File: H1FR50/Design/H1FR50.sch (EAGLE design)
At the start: 49 parts, among them P1 HEXABIT_17.32_NO_P6, U1 STM32F091CBU6, U2 TPS22943DCKR, U3 BGA824N6, U4 TESEO-LIV3F, U5 B39162B4327P810, X1 XTALL_CSTCE8M00G52

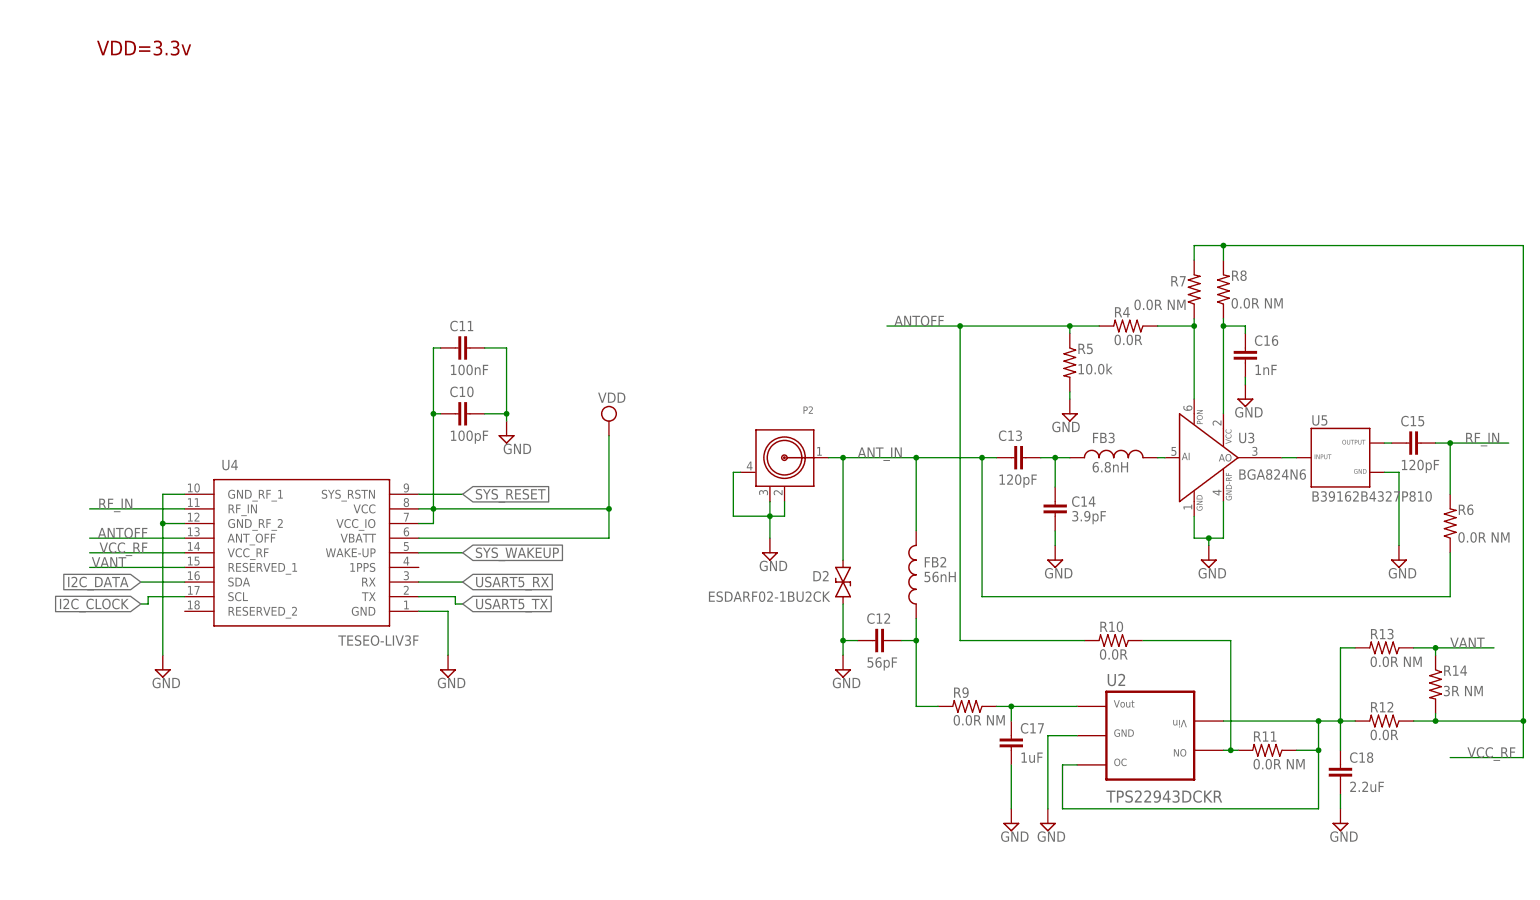
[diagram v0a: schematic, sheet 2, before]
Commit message: - Rearanged all P#.. - Removed Keepout areas.. - Renamed all NM to DNP.. - Moved D1 from layer 16 to layer 1.. - Changed R8 from 0R NM to 0R.. - Placed more Grounding vias around RF connector in brd.. - Added two pullups res on I2C lines.. - Added the recomended filters on Tevo's power pins.. - Updated Document.. - Updated BOM..
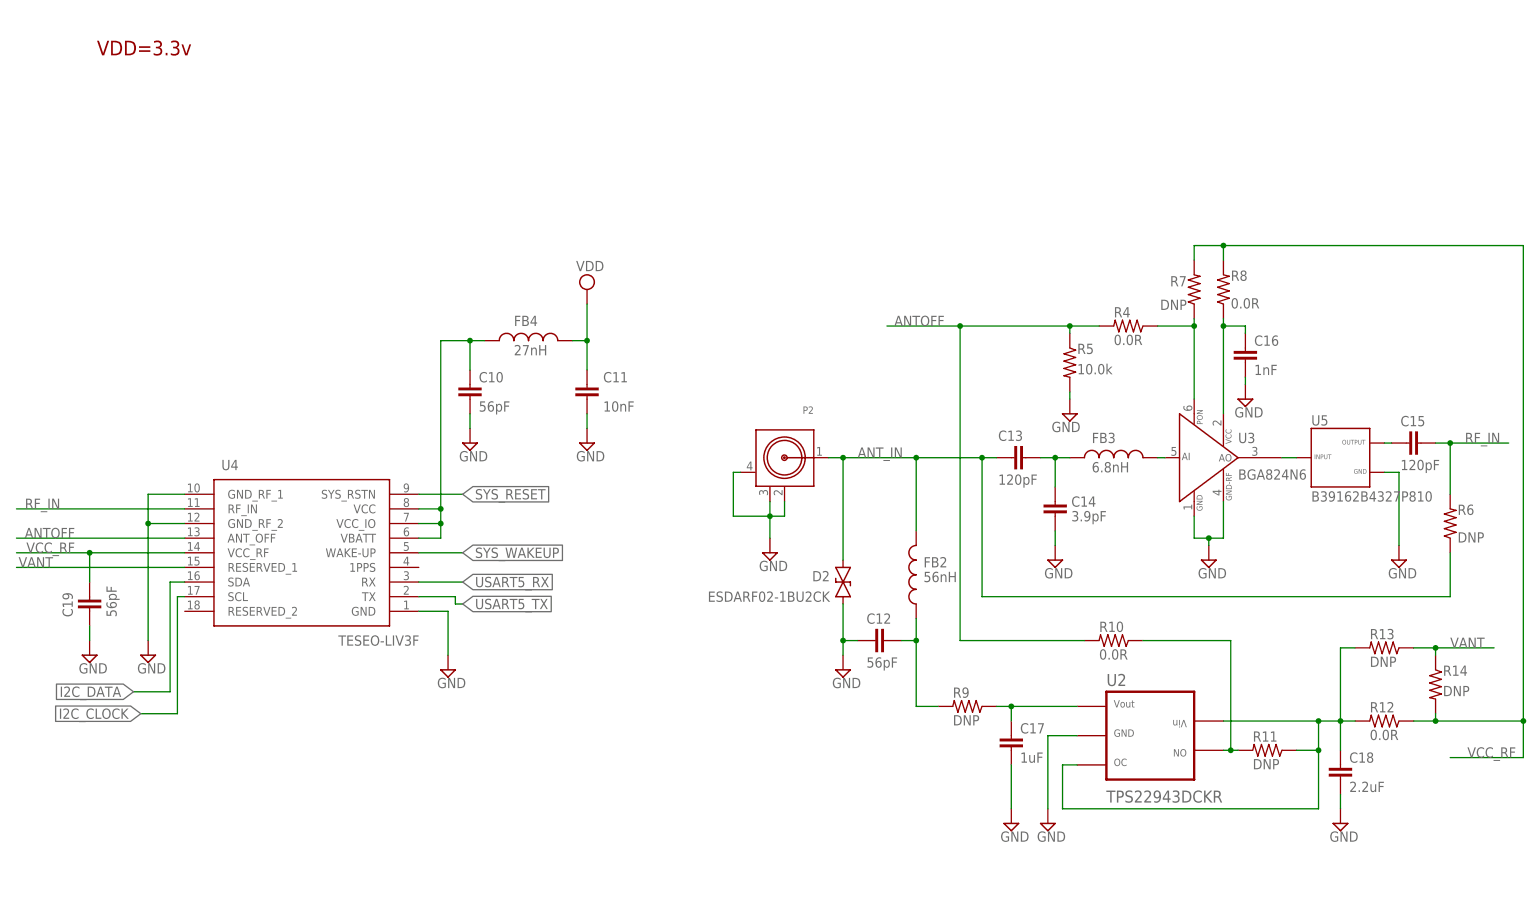
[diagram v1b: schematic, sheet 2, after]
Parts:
- added C19: 56pF, HEXABITZ_RCLS:C-0402
- added FB4: 27nH, HEXABITZ_RCLS:FB-0402
- added R15, R16: 2.2k, HEXABITZ_RCLS:R-0402
- C10: value 100pF -> 56pF
- C11: value 100nF -> 10nF
- R11, R13, R6, R7, R9: value 0.0R NM -> DNP
- R14: value 3R NM -> DNP
- R8: value 0.0R NM -> 0.0R
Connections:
- new net VCC_RF1: C10.2, FB4.1, U4.VBATT, U4.VCC, U4.VCC_IO
- net GND: now also C10.1, C11.1, C19.1; no longer C10.2, C11.2
- net I2C_CLOCK: now also R15.2
- net I2C_DATA: now also R16.2
- net VCC_RF: now also C19.2
- net VDD: now also C11.2, FB4.2, R15.1, R16.1; no longer C10.1, C11.1, U4.VBATT, U4.VCC, U4.VCC_IO
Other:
- moved on the sheet: C10, C11

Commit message: - Redesigned both Schematic and PCB.. - Updated BOM and Documentation..
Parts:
- removed FB1: FB-TDK_MMZ1608Y300B, Hexabitz:FB-TDK_MMZ1608Y300B
- removed R15, R16: 2.2k, HEXABITZ_RCLS:R-0402
- removed R3: 0.0R, Hexabitz:R-0603
- C1: value 100nF -> 10nF; CAPACITANCE 100nF -> 10nF; MFN AVX -> KEMET; MPN 0603YC104K4T2A -> C0603C103K5RACTU; OCTOPART_URL https://octopart.com/c0603c104k8ractu-kemet-145075?r=sp&s=9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 -> https://octopart.com/c0603c103k5ractu-kemet-133094?r=sp&s=R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; VOLTAGE_RATING 16V -> 50V
- C10, C19: device HEXABITZ_RCLS:C-0402 -> HEXABITZ_RCLS:C-0201C0201; MFN (none) -> Murata; MPN (none) -> GRM0335C1E560GA01D; OCTOPART_URL (none) -> https://octopart.com/grm0335c1e560ga01d-murata-24611383?r=sp
- C11: CAPACITANCE (none) -> 10nF; MFN (none) -> TDK; MPN (none) -> CGA2B3X7R1H103K050BE; OCTOPART_URL (none) -> https://octopart.com/cga2b3x7r1h103k050be-tdk-68305469?r=sp
- C12: CAPACITANCE (none) -> 56pF; MFN (none) -> Murata; MPN (none) -> GRM1555C1H560JA01D; OCTOPART_URL (none) -> https://octopart.com/grm1555c1h560ja01d-murata-15197568?r=sp
- C13, C15: CAPACITANCE (none) -> 120pF; MFN (none) -> Murata; MPN (none) -> GRM1555C1H121JA01D; OCTOPART_URL (none) -> https://octopart.com/grm1555c1h121ja01d-murata-196010?r=sp
- C14: CAPACITANCE (none) -> 3.9pF; MFN (none) -> Murata; MPN (none) -> GRM1555C1H3R9WA01D; OCTOPART_URL (none) -> https://octopart.com/grm1555c1h3r9wa01d-murata-20477997?r=sp
- C16: CAPACITANCE (none) -> 1nF; MFN (none) -> Murata; MPN (none) -> GRM155R71H102KA01D; OCTOPART_URL (none) -> https://octopart.com/grm155r71h102ka01d-murata-196021?r=sp
- C17: value 1uF -> 1.00uF; CAPACITANCE (none) -> 1.00uF; MFN (none) -> KEMET; MPN (none) -> C0402C105K8PAC7411; OCTOPART_URL (none) -> https://octopart.com/c0402c105k8pac7411-kemet-75146233?r=sp
- C18: CAPACITANCE (none) -> 2.2uF; MFN (none) -> https://octopart.com/c0402c225k7pactu-kemet-89187402?r=sp; MPN (none) -> C0402C225K7PACTU; OCTOPART_URL (none) -> https://octopart.com/c0402c225k7pactu-kemet-89187402?r=sp
- C2: MFN AVX -> Yageo; MPN TAJR105M016RNJ -> CC0805KKX7R7BB105; OCTOPART_URL https://octopart.com/tajr105m016rnj-avx-1188552 -> https://octopart.com/cc0805kkx7r7bb105-yageo-8376555?r=sp&s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; TOLERANCE 20% -> 10%
- C3: value 4.7uF -> 100nF; device Hexabitz:C-0805-POL -> Hexabitz:C-0603; CAPACITANCE 4.7uF -> 100nF; MFN Panasonic -> KEMET; MPN 10TPU4R7MSI -> C0603C104K8RACTU; OCTOPART_URL https://octopart.com/10tpu4r7msi-panasonic-29487748 -> https://octopart.com/c0603c104k8ractu-kemet-145075?r=sp&s=9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; TOLERANCE 20% -> 10%
- C4: MFN Panasonic -> Murata; MPN 10TPU4R7MSI -> GRM21BC81E475KA12L; OCTOPART_URL https://octopart.com/10tpu4r7msi-panasonic-29487748 -> https://octopart.com/grm21bc81e475ka12l-murata-10331911?r=s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; TOLERANCE 20% -> 10%; VOLTAGE_RATING 10V -> 25V
- C5: value 10nF -> 100nF; CAPACITANCE 10nF -> 100nF; MFN AVX -> KEMET; MPN 0603YC103KAT4A -> C0603C104K8RACTU; OCTOPART_URL https://octopart.com/0603yc103kat4a-avx-2550362 -> https://octopart.com/c0603c104k8ractu-kemet-145075?r=sp&s=9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; VOLTAGE_RATING 16V -> 10
- C6, C8: MFN AVX -> KEMET; MPN 0603YC104K4T2A -> C0603C104K8RACTU; OCTOPART_URL https://octopart.com/0603yc104k4t2a-avx-8120651# -> https://octopart.com/c0603c104k8ractu-kemet-145075?r=sp&s=9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; VOLTAGE_RATING 16V -> 10V
- C7: value 100nF -> 4.7uF; device Hexabitz:C-0603 -> Hexabitz:C-0805-POL; CAPACITANCE 100nF -> 4.7uF; MFN AVX -> Murata; MPN 0603YC104K4T2A -> GRM21BC81E475KA12L; OCTOPART_URL https://octopart.com/0603yc104k4t2a-avx-8120651# -> https://octopart.com/grm21bc81e475ka12l-murata-10331911?r=s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; VOLTAGE_RATING 16V -> 25V
- C9: MFN AVX -> KEMET; MPN 0603YC104K4T2A -> C0603C104K8RACTU; OCTOPART_URL https://octopart.com/0603yc104k4t2a-avx-8120651# -> https://octopart.com/c0603c104k8ractu-kemet-145075?r=sp&s=9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; TOLERANCE 10% -> 10V; VOLTAGE_RATING 16V -> 10%
- FB2: MFN (none) -> Murata; MPN (none) -> LQW15AN6N8G00D; OCTOPART_URL (none) -> https://octopart.com/lqw15an6n8g00d-murata-7896134?r=sp
- FB3: MFN (none) -> Würth Elektronik; MPN (none) -> 744784156A; OCTOPART_URL (none) -> https://octopart.com/744784156a-w%C3%BCrth+elektronik-46756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
- FB4: MFN (none) -> Murata; MPN (none) -> LQG15HS27NJ02D; OCTOPART_URL (none) -> https://octopart.com/lqg15hs27nj02d-murata-387555?r=sp
- P1: value HEXABIT_17.32_NO_P6 -> HEXABIT_17.32_X2_NO_P5; device hexabitz_connectors:HEXABIT_17.32_NO_P6 -> hexabitz_connectors:HEXABIT_17.32_X2_NO_P5
- R14: value DNP -> 100k; device HEXABITZ_RCLS:R-0402 -> HEXABITZ_RCLS:R-0603; MFN (none) -> Yageo; MPN (none) -> AC0603FR-07100KL; OCTOPART_URL (none) -> https://octopart.com/ac0603fr-07100kl-yageo-21711090?r=sp; RESISTANCE (none) -> 100k; TOLERANCE (none) -> ±1%
- R2: MFN Vishay -> Yageo; MPN CRCW060310K0JNEB -> RC0603JR-0710KL; OCTOPART_URL https://octopart.com/crcw060310k0jneb-vishay-46603269 -> https://octopart.com/search?q=RC0603JR-0710KL&start=0
- R5: MFN (none) -> TE Connectivity; MPN (none) -> CRGCQ0402F10K; OCTOPART_URL (none) -> https://octopart.com/crgcq0402f10k-te+connectivity-91017932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; RESISTANCE (none) -> 10.0K; TOLERANCE (none) -> ±1%
- U1: value STM32F091CBU6 -> STM32F091RBT6STMICROELECTRONICS_STM32F091RBT6_0_1; device Hexabitz:STM32F091CBU6 -> Hexabitz:STM32F091RBT6STMICROELECTRONICS_STM32F091RBT6_0_1; MFN (none) -> STMicroelectronics; OCTOPART_URL (none) -> https://octopart.com/stm32f091rbt6-stmicroelectronics-51988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
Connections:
- removed net USART1_RX: P1.SD5, U1.PA10
- removed net USART1_TX: P1.SU5, U1.PA9
- removed net USART2_RX: P1.SD2, U1.PA3
- removed net USART2_TX: P1.SU2, U1.PA2
- removed net USART3_RX: P1.SD4, U1.PB11
- removed net USART3_TX: P1.SU4, U1.PB10
- removed net USART4_RX: P1.SD1, U1.PA1
- removed net USART4_TX: P1.SU1, U1.PA0
- removed net USART5_RX: U1.PB4, U4.RX
- removed net USART5_TX: U1.PB3, U4.TX
- removed net USART6_RX: P1.SD3, U1.PA5
- removed net USART6_TX: P1.SU3, U1.PA4
- removed net VANT: R13.1, R14.1, U4.RESERVED_1
- removed net VDDA: C2.+, C5.1, FB1.1, U1.VDDA
- removed net VSSA: C2.-, C5.2, R3.2, U1.VSS_A
- new net N$2: R14.2, U2.OC
- new net N$3: C13.1, D2.2, FB2.2, P2.1, R13.2
- new net UART1_RX*: P1.SD7, U1.PA10
- new net UART1_TX*: P1.SU7, U1.PA9
- new net UART2_RX*: P1.SD3, U1.PA3
- new net UART2_TX*: P1.SU3, U1.PA2
- new net UART3_RX: U1.PB11, U4.RX
- new net UART3_TX: U1.PB10, U4.TX
- new net UART4_RX: P1.SD2, U1.PA1
- new net UART4_TX: P1.SU2, U1.PA0
- new net UART5_RX: P1.SD8, U1.PB4
- new net UART5_TX: P1.SU8, U1.PB3
- new net UART6_RX: P1.SD10, U1.PA5
- new net UART6_TX: P1.SU10, U1.PA4
- new net UART7_RX: P1.SD9, U1.PC1
- new net UART7_TX: P1.SU9, U1.PC0
- new net UART8_RX: P1.SD1, U1.PC3
- new net UART8_TX: P1.SU1, U1.PC2
- net ANT_IN: now also R13.1; no longer C13.1, D2.2, FB2.2, P2.1
- net B1: now also U1.PF11-BOOT0; no longer U1.PF11-OSC_BOOT0
- net GND: now also C2.-, C3.2, C5.2, C7.-, P1.GND10, P1.GND7, P1.GND9, U1.1_VSS, U1.2_VSS, U1.3_VSS, U1.4_VSS, U1.VSSA; no longer C3.-, C7.2, P1.GND3, R3.1, U1.EP, U1.VSS_0, U1.VSS_1, U1.VSS_2
- net I2C_CLOCK: no longer R15.2
- net I2C_DATA: no longer R16.2
- net N$23: now also R14.1; no longer R13.2, U2.OC
- net N$5: now also U1.PF0-OSC_IN(PF0); no longer U1.PF0-OSC_IN
- net N$6: now also U1.PF1-OSC_OUT(PF1); no longer U1.PF1-OSC_OUT
- net R1: now also C8.1; no longer C1.1
- net VCC_RF: no longer R14.2
- net VDD: now also C1.1, C2.+, C3.1, C5.1, C7.+, P1.VDD10, P1.VDD7, P1.VDD9, U1.1_VDD, U1.2_VDD, U1.3_VDD, U1.VDDA; no longer C3.+, C7.1, C8.1, FB1.2, P1.VDD3, R15.1, R16.1, U1.VDD_0, U1.VDD_1
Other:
- moved on the sheet: B, C, C1, C19, C2, C4, C5, C6, C8, C9, D, D1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

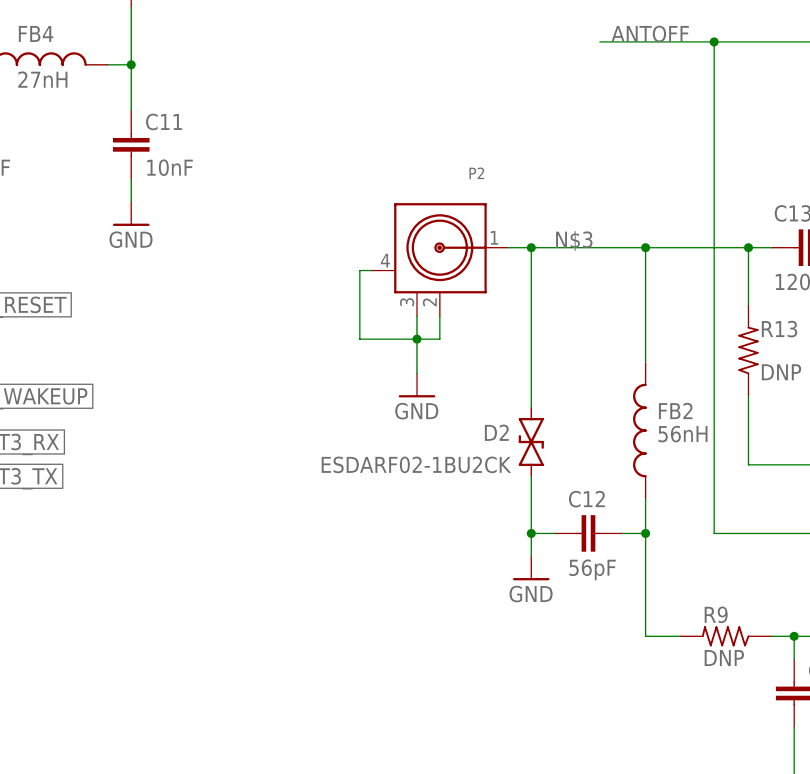
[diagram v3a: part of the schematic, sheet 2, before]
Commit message: - Changed RF Connector.. - Documents and BOM were updated..
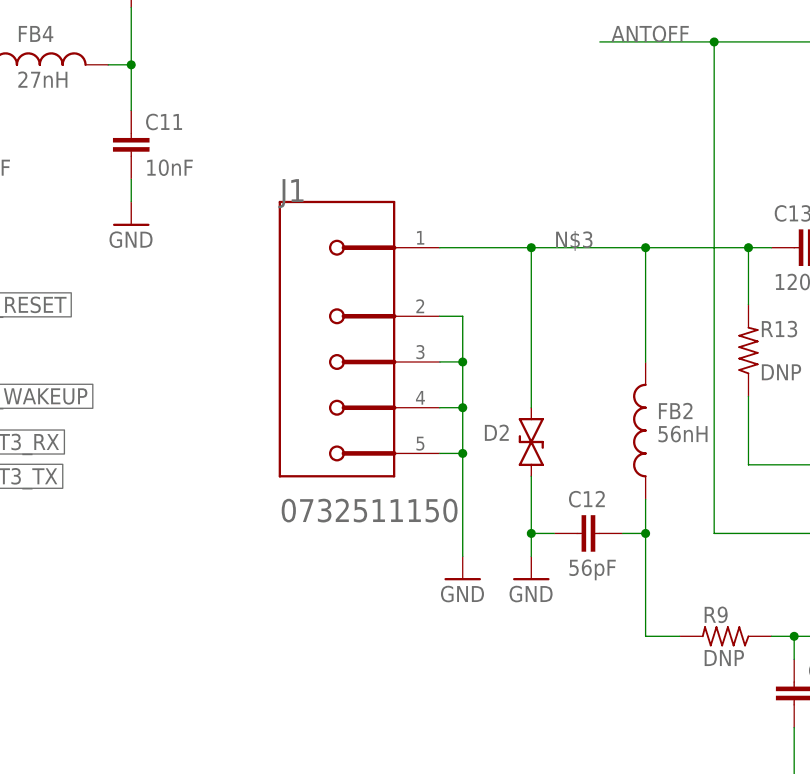
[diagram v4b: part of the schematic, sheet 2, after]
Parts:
- removed P2: (no value), HEXABITZ_CONNECTION_PARTS:0734120110
- added J1: MOLEX_INC_0732511150MOLEX_INC_0732511150_0_0, HEXABITZ_CONNECTION_PARTS:MOLEX_INC_0732511150MOLEX_INC_0732511150_0_0
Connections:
- net GND: now also J1.MNT_1, J1.MNT_2, J1.MNT_3, J1.MNT_4; no longer P2.2, P2.3, P2.4
- net N$3: now also J1.1; no longer P2.1
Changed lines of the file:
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@@
 </part>
 <part name="R12" library="HEXABITZ_RCLS" library_urn="urn:adsk.eagle:library:20064561" deviceset="R-0402" device="" package3d_urn="urn:adsk.eagle:package:19666455/2" value="0.0R"/>
-<part name="P2" library="HEXABITZ_CONNECTION_PARTS" library_urn="urn:adsk.eagle:library:20064553" deviceset="0734120110" device="" package3d_urn="urn:adsk.eagle:package:19666477/2"/>
 <part name="C19" library="HEXABITZ_RCLS" library_urn="urn:adsk.eagle:library:20064561" deviceset="C-0201" device="C0201" package3d_urn="urn:adsk.eagle:package:27626996/2" value="56pF">
 <spice>
@@
 <part name="GND23" library="supply1" library_urn="urn:adsk.eagle:library:371" deviceset="GND" device=""/>
 <part name="GND24" library="supply1" library_urn="urn:adsk.eagle:library:371" deviceset="GND" device=""/>
+<part name="J1" library="HEXABITZ_CONNECTION_PARTS" library_urn="urn:adsk.eagle:library:20064553" deviceset="MOLEX_INC_0732511150" device="MOLEX_INC_0732511150_0_0" package3d_urn="urn:adsk.eagle:package:27877899/1"/>
 </parts>
 <sheets>
@@
 <instance part="D2" gate="G$1" x="152.4" y="102.87" smashed="yes" rot="R90">
 <attribute name="NAME" x="150.114" y="106.045" size="1.778" layer="95" rot="R180"/>
-<attribute name="VALUE" x="150.114" y="102.489" size="1.778" layer="96" rot="R180"/>
 </instance>
 <instance part="C12" gate="G$1" x="160.02" y="93.98" smashed="yes" rot="R90">
@@
 <attribute name="VALUE" x="243.84" y="76.708" size="1.778" layer="96"/>
 </instance>
-<instance part="P2" gate="G$1" x="142.24" y="125.73" smashed="yes" rot="MR0">
-<attribute name="NAME" x="147.32" y="133.35" size="1.27" layer="95" rot="MR0"/>
-<attribute name="VALUE" x="147.32" y="130.81" size="1.27" layer="96" rot="MR0"/>
-</instance>
 <instance part="C19" gate="G$1" x="21.59" y="101.6" smashed="yes" rot="R180">
 <attribute name="NAME" x="23.114" y="104.521" size="1.778" layer="95"/>
@@
 <attribute name="VALUE" x="105.41" y="125.73" size="1.778" layer="96"/>
 </instance>
-<instance part="GND6" gate="1" x="139.7" y="109.22" smashed="yes">
-<attribute name="VALUE" x="137.16" y="106.68" size="1.778" layer="96"/>
+<instance part="GND6" gate="1" x="144.78" y="88.9" smashed="yes">
+<attribute name="VALUE" x="142.24" y="86.36" size="1.778" layer="96"/>
 </instance>
 <instance part="GND7" gate="1" x="152.4" y="88.9" smashed="yes">
@@
 <attribute name="VALUE" x="246.38" y="105.41" size="1.778" layer="96"/>
 </instance>
+<instance part="J1" gate="G$0" x="121.92" y="135.89" smashed="yes">
+<attribute name="NAME" x="124.46" y="133.35" size="2.54" layer="95" align="top-left"/>
+</instance>
 </instances>
 <busses>
@@
 <wire x1="176.53" y1="125.73" x2="165.1" y2="125.73" width="0.1524" layer="91"/>
 <wire x1="165.1" y1="125.73" x2="152.4" y2="125.73" width="0.1524" layer="91"/>
-<pinref part="P2" gate="G$1" pin="1"/>
-<wire x1="149.86" y1="125.73" x2="152.4" y2="125.73" width="0.1524" layer="91"/>
 <junction x="152.4" y="125.73"/>
 <pinref part="D2" gate="G$1" pin="2"/>
@@
 <wire x1="176.53" y1="119.38" x2="176.53" y2="125.73" width="0.1524" layer="91"/>
 <junction x="176.53" y="125.73"/>
+<pinref part="J1" gate="G$0" pin="1"/>
+<wire x1="142.24" y1="125.73" x2="152.4" y2="125.73" width="0.1524" layer="91"/>
 </segment>
 </net>
@@
 </segment>
 <segment>
-<wire x1="139.7" y1="111.76" x2="139.7" y2="115.57" width="0.1524" layer="91"/>
-<wire x1="139.7" y1="115.57" x2="139.7" y2="118.11" width="0.1524" layer="91"/>
-<wire x1="142.24" y1="118.11" x2="142.24" y2="115.57" width="0.1524" layer="91"/>
-<wire x1="142.24" y1="115.57" x2="139.7" y2="115.57" width="0.1524" layer="91"/>
-<junction x="139.7" y="115.57"/>
-<wire x1="139.7" y1="115.57" x2="133.35" y2="115.57" width="0.1524" layer="91"/>
-<wire x1="133.35" y1="115.57" x2="133.35" y2="123.19" width="0.1524" layer="91"/>
-<pinref part="P2" gate="G$1" pin="2"/>
-<pinref part="P2" gate="G$1" pin="3"/>
-<pinref part="P2" gate="G$1" pin="4"/>
-<wire x1="134.62" y1="123.19" x2="133.35" y2="123.19" width="0.1524" layer="91"/>
-<pinref part="GND6" gate="1" pin="GND"/>
-</segment>
-<segment>
 <pinref part="C12" gate="G$1" pin="1"/>
 <pinref part="D2" gate="G$1" pin="1"/>
@@
 <pinref part="GND15" gate="1" pin="GND"/>
 </segment>
+<segment>
+<pinref part="GND6" gate="1" pin="GND"/>
+<pinref part="J1" gate="G$0" pin="MNT_1"/>
+<wire x1="144.78" y1="91.44" x2="144.78" y2="102.87" width="0.1524" layer="91"/>
+<wire x1="144.78" y1="102.87" x2="144.78" y2="107.95" width="0.1524" layer="91"/>
+<wire x1="144.78" y1="107.95" x2="144.78" y2="113.03" width="0.1524" layer="91"/>
+<wire x1="144.78" y1="113.03" x2="144.78" y2="118.11" width="0.1524" layer="91"/>
+<wire x1="144.78" y1="118.11" x2="142.24" y2="118.11" width="0.1524" layer="91"/>
+<pinref part="J1" gate="G$0" pin="MNT_2"/>
+<wire x1="142.24" y1="113.03" x2="144.78" y2="113.03" width="0.1524" layer="91"/>
+<junction x="144.78" y="113.03"/>
+<pinref part="J1" gate="G$0" pin="MNT_3"/>
+<wire x1="142.24" y1="107.95" x2="144.78" y2="107.95" width="0.1524" layer="91"/>
+<junction x="144.78" y="107.95"/>
+<pinref part="J1" gate="G$0" pin="MNT_4"/>
+<wire x1="142.24" y1="102.87" x2="144.78" y2="102.87" width="0.1524" layer="91"/>
+<junction x="144.78" y="102.87"/>
+</segment>
 </net>
